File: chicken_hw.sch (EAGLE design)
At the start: 20 parts, among them U1 MUX-74HC4067SMD

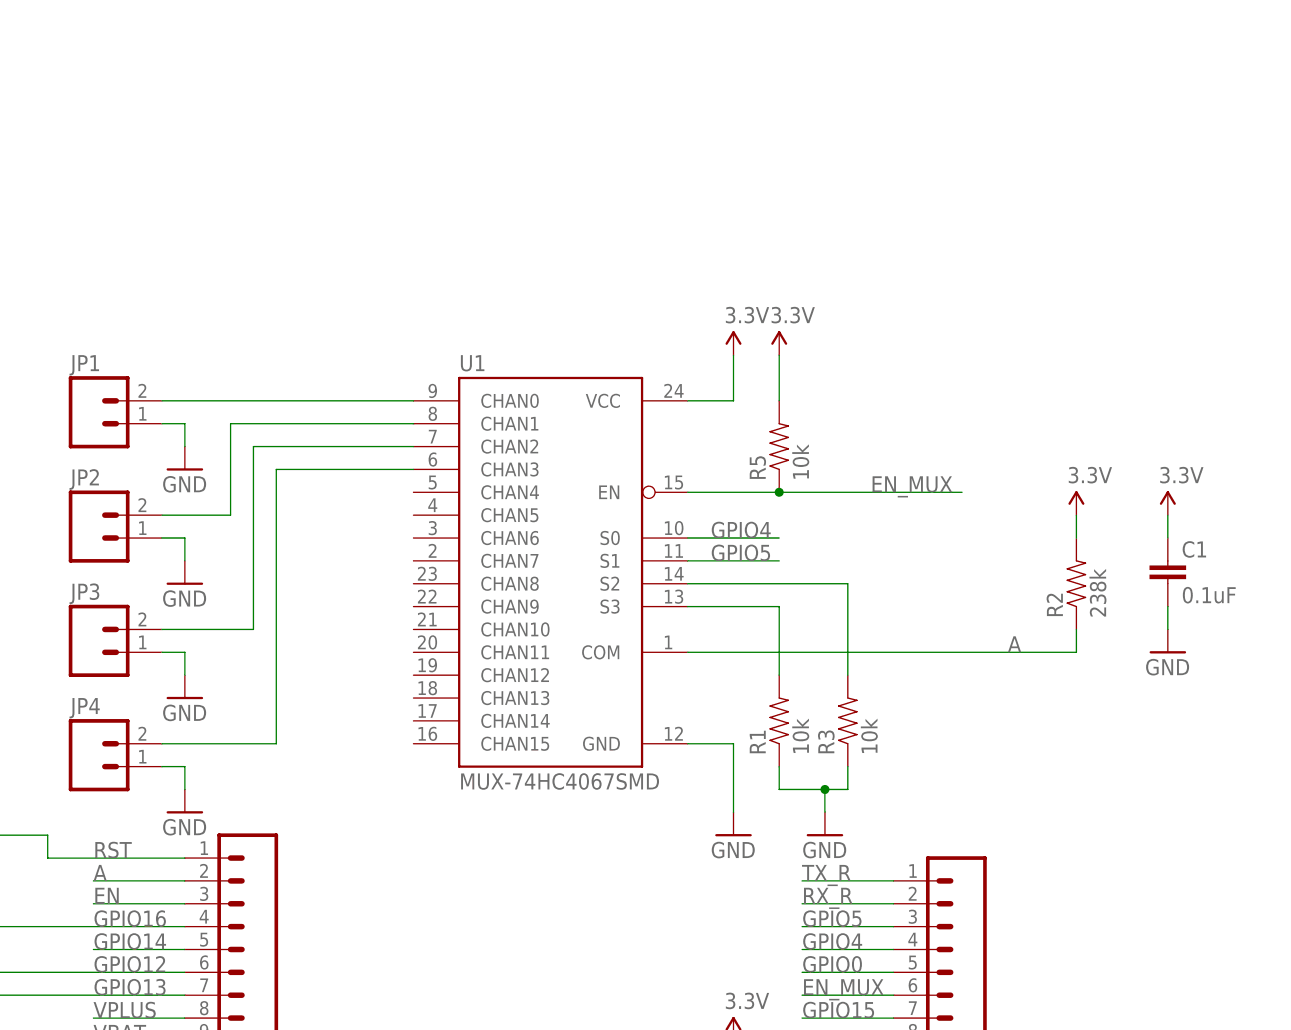
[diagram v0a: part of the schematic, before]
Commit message: Switch to 8to1 mux to save on cost
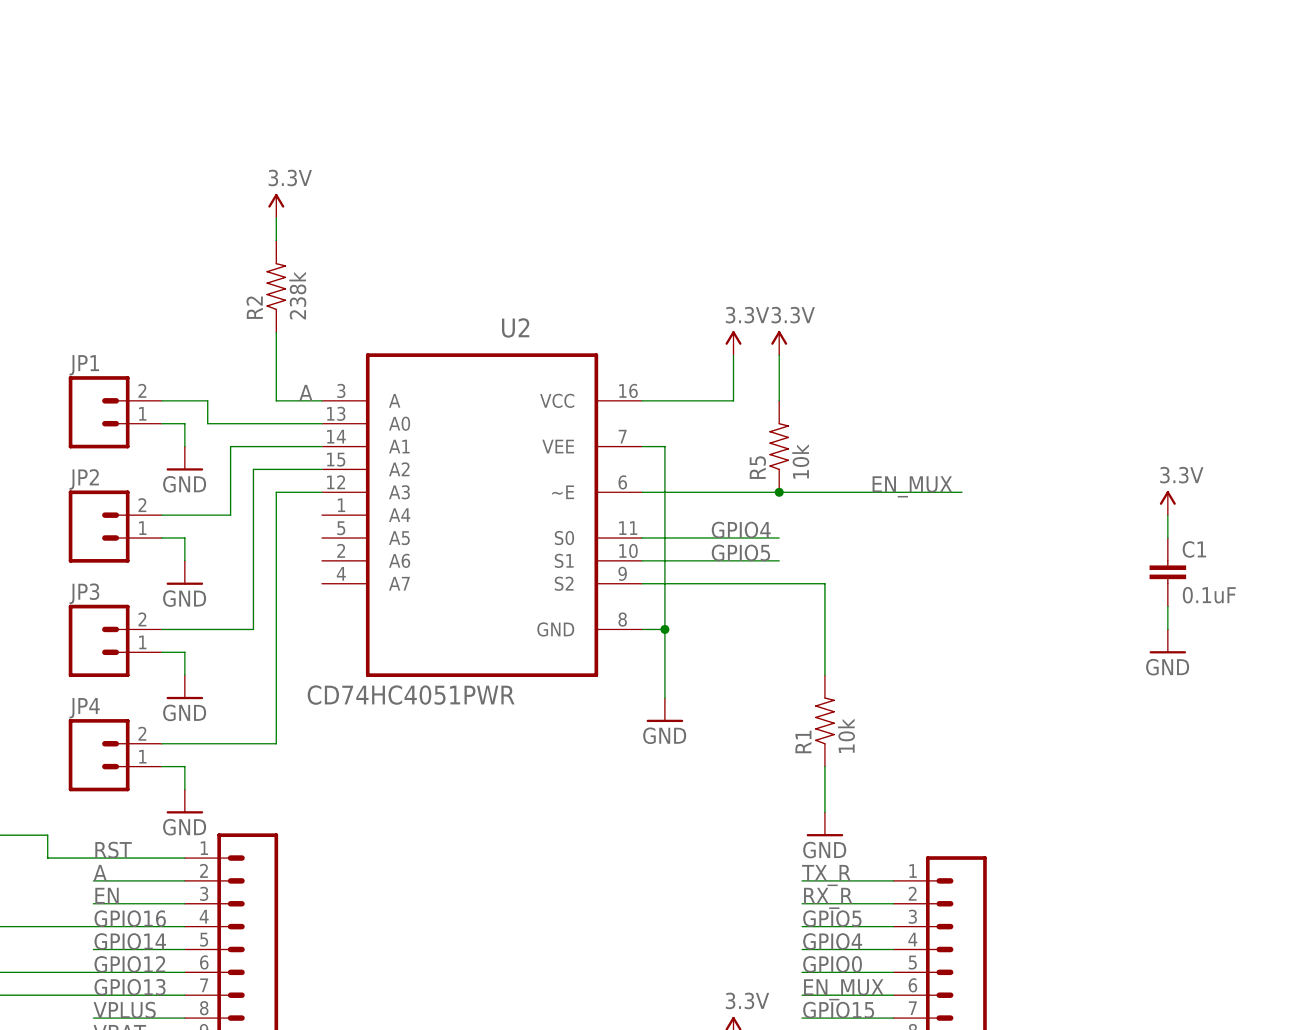
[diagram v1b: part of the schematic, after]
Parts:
- removed R3: 10k, SparkFun-Resistors:RESISTOR0603
- removed U1: MUX-74HC4067SMD, SparkFun-AnalogIC:MUX-74HC4067SMD
- added U2: CD74HC4051PWR, Texas Instruments_By_element14_Batch_1:CD74HC4051PWR
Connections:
- removed net N$6: R3.2, U1.S2
- net 3.3V: no longer U1.VCC
- net A: now also U2.A; no longer U1.COM
- net EN_MUX: now also U2.~E; no longer U1.EN
- net GND: now also U2.GND, U2.VEE; no longer R3.1, U1.GND
- net GPIO4: now also U2.S0; no longer U1.S0
- net GPIO5: now also U2.S1; no longer U1.S1
- net N$1: no longer U1.S3
- net N$2: now also U2.A0; no longer U1.CHAN0
- net N$3: now also U2.A1; no longer U1.CHAN1
- net N$4: now also U2.A2; no longer U1.CHAN2
- net N$5: now also U2.A3; no longer U1.CHAN3
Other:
- moved on the sheet: R1, R2
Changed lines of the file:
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@@
 <part name="GND3" library="SparkFun-Aesthetics" deviceset="GND" device=""/>
 <part name="SUPPLY1" library="SparkFun-Aesthetics" deviceset="3.3V" device=""/>
-<part name="U1" library="SparkFun-AnalogIC" deviceset="MUX-74HC4067" device="SMD"/>
 <part name="SUPPLY2" library="SparkFun-Aesthetics" deviceset="3.3V" device=""/>
 <part name="GND4" library="SparkFun-Aesthetics" deviceset="GND" device=""/>
@@
 <part name="R5" library="SparkFun-Resistors" deviceset="RESISTOR" device="0603" value="10k"/>
 <part name="R1" library="SparkFun-Resistors" deviceset="RESISTOR" device="0603" value="10k"/>
-<part name="R3" library="SparkFun-Resistors" deviceset="RESISTOR" device="0603" value="10k"/>
 <part name="R2" library="SparkFun-Resistors" deviceset="RESISTOR" device="0603" value="238k"/>
 <part name="D1" library="SparkFun-LED" deviceset="LED-GREEN" device="0603" value="GREEN"/>
@@
 <part name="LOGO1" library="SparkFun-Aesthetics" deviceset="OSHW-LOGO" device="S"/>
 <part name="DS" library="SparkFun-Passives" deviceset="JUMPER-PAD-2-NC_BY_TRACE" device=""/>
+<part name="U2" library="Texas Instruments_By_element14_Batch_1" deviceset="CD74HC4051PWR" device=""/>
 </parts>
 <sheets>
@@
 <instance part="GND3" gate="1" x="-15.24" y="17.78"/>
 <instance part="SUPPLY1" gate="G$1" x="60.96" y="25.4"/>
-<instance part="U1" gate="G$1" x="40.64" y="78.74"/>
 <instance part="SUPPLY2" gate="G$1" x="60.96" y="101.6"/>
-<instance part="GND4" gate="1" x="60.96" y="48.26"/>
+<instance part="GND4" gate="1" x="53.34" y="60.96"/>
 <instance part="SUPPLY3" gate="G$1" x="66.04" y="101.6"/>
-<instance part="SUPPLY4" gate="G$1" x="99.06" y="83.82"/>
+<instance part="SUPPLY4" gate="G$1" x="10.16" y="116.84"/>
 <instance part="JP1" gate="G$1" x="-10.16" y="93.98"/>
 <instance part="JP2" gate="G$1" x="-10.16" y="81.28"/>
@@
 <instance part="C1" gate="G$1" x="109.22" y="76.2"/>
 <instance part="R5" gate="G$1" x="66.04" y="91.44" rot="R90"/>
-<instance part="R1" gate="G$1" x="66.04" y="60.96" rot="R90"/>
-<instance part="R3" gate="G$1" x="73.66" y="60.96" rot="R90"/>
-<instance part="R2" gate="G$1" x="99.06" y="76.2" rot="R90"/>
+<instance part="R1" gate="G$1" x="71.12" y="60.96" rot="R90"/>
+<instance part="R2" gate="G$1" x="10.16" y="109.22" rot="R90"/>
 <instance part="D1" gate="G$1" x="-53.34" y="10.16"/>
 <instance part="D2" gate="G$1" x="-40.64" y="10.16"/>
@@
 <instance part="LOGO1" gate="G$1" x="137.16" y="12.7"/>
 <instance part="DS" gate="G$1" x="-27.94" y="43.18" rot="R90"/>
+<instance part="U2" gate="A" x="33.02" y="86.36" rot="MR0"/>
 </instances>
 <busses>
@@
 </segment>
 <segment>
-<pinref part="U1" gate="G$1" pin="COM"/>
-<wire x1="55.88" y1="68.58" x2="99.06" y2="68.58" width="0.1524" layer="91"/>
-<label x="91.44" y="68.58" size="1.778" layer="95"/>
-<wire x1="99.06" y1="68.58" x2="99.06" y2="71.12" width="0.1524" layer="91"/>
+<wire x1="10.16" y1="96.52" x2="10.16" y2="104.14" width="0.1524" layer="91"/>
+<label x="12.7" y="96.52" size="1.778" layer="95"/>
 <pinref part="R2" gate="G$1" pin="1"/>
+<pinref part="U2" gate="A" pin="A"/>
+<wire x1="10.16" y1="96.52" x2="15.24" y2="96.52" width="0.1524" layer="91"/>
 </segment>
 </net>
@@
 </segment>
 <segment>
-<pinref part="U1" gate="G$1" pin="S0"/>
-<wire x1="55.88" y1="81.28" x2="66.04" y2="81.28" width="0.1524" layer="91"/>
+<wire x1="50.8" y1="81.28" x2="66.04" y2="81.28" width="0.1524" layer="91"/>
 <label x="58.42" y="81.28" size="1.778" layer="95"/>
+<pinref part="U2" gate="A" pin="S0"/>
 </segment>
 </net>
@@
 </segment>
 <segment>
-<pinref part="U1" gate="G$1" pin="S1"/>
-<wire x1="55.88" y1="78.74" x2="66.04" y2="78.74" width="0.1524" layer="91"/>
+<wire x1="50.8" y1="78.74" x2="66.04" y2="78.74" width="0.1524" layer="91"/>
 <label x="58.42" y="78.74" size="1.778" layer="95"/>
+<pinref part="U2" gate="A" pin="S1"/>
 </segment>
 </net>
@@
 </segment>
 <segment>
-<pinref part="U1" gate="G$1" pin="GND"/>
-<wire x1="55.88" y1="58.42" x2="60.96" y2="58.42" width="0.1524" layer="91"/>
-<pinref part="GND4" gate="1" pin="GND"/>
-<wire x1="60.96" y1="58.42" x2="60.96" y2="50.8" width="0.1524" layer="91"/>
-</segment>
-<segment>
 <pinref part="JP1" gate="G$1" pin="1"/>
 <wire x1="-2.54" y1="93.98" x2="0" y2="93.98" width="0.1524" layer="91"/>
@@
 </segment>
 <segment>
-<wire x1="66.04" y1="55.88" x2="66.04" y2="53.34" width="0.1524" layer="91"/>
-<wire x1="66.04" y1="53.34" x2="71.12" y2="53.34" width="0.1524" layer="91"/>
 <pinref part="GND9" gate="1" pin="GND"/>
-<wire x1="71.12" y1="53.34" x2="73.66" y2="53.34" width="0.1524" layer="91"/>
-<wire x1="73.66" y1="53.34" x2="73.66" y2="55.88" width="0.1524" layer="91"/>
-<wire x1="71.12" y1="50.8" x2="71.12" y2="53.34" width="0.1524" layer="91"/>
-<junction x="71.12" y="53.34"/>
+<wire x1="71.12" y1="50.8" x2="71.12" y2="55.88" width="0.1524" layer="91"/>
 <pinref part="R1" gate="G$1" pin="1"/>
-<pinref part="R3" gate="G$1" pin="1"/>
 </segment>
 <segment>
@@
 <wire x1="-40.64" y1="0" x2="-40.64" y2="5.08" width="0.1524" layer="91"/>
 </segment>
+<segment>
+<pinref part="U2" gate="A" pin="GND"/>
+<wire x1="50.8" y1="71.12" x2="53.34" y2="71.12" width="0.1524" layer="91"/>
+<pinref part="GND4" gate="1" pin="GND"/>
+<wire x1="53.34" y1="71.12" x2="53.34" y2="63.5" width="0.1524" layer="91"/>
+<wire x1="53.34" y1="71.12" x2="53.34" y2="91.44" width="0.1524" layer="91"/>
+<junction x="53.34" y="71.12"/>
+<pinref part="U2" gate="A" pin="VEE"/>
+<wire x1="53.34" y1="91.44" x2="50.8" y2="91.44" width="0.1524" layer="91"/>
+</segment>
 </net>
 <net name="N$11" class="0">
@@
 </segment>
 <segment>
-<pinref part="U1" gate="G$1" pin="VCC"/>
-<wire x1="55.88" y1="96.52" x2="60.96" y2="96.52" width="0.1524" layer="91"/>
+<wire x1="50.8" y1="96.52" x2="60.96" y2="96.52" width="0.1524" layer="91"/>
 <pinref part="SUPPLY2" gate="G$1" pin="3.3V"/>
 <wire x1="60.96" y1="96.52" x2="60.96" y2="101.6" width="0.1524" layer="91"/>
@@
 <segment>
 <pinref part="SUPPLY4" gate="G$1" pin="3.3V"/>
-<wire x1="99.06" y1="83.82" x2="99.06" y2="81.28" width="0.1524" layer="91"/>
+<wire x1="10.16" y1="116.84" x2="10.16" y2="114.3" width="0.1524" layer="91"/>
 <pinref part="R2" gate="G$1" pin="2"/>
 </segment>
@@
 <net name="EN_MUX" class="0">
 <segment>
-<pinref part="U1" gate="G$1" pin="EN"/>
-<wire x1="55.88" y1="86.36" x2="66.04" y2="86.36" width="0.1524" layer="91"/>
+<wire x1="50.8" y1="86.36" x2="66.04" y2="86.36" width="0.1524" layer="91"/>
 <label x="76.2" y="86.36" size="1.778" layer="95"/>
 <pinref part="R5" gate="G$1" pin="1"/>
 <wire x1="66.04" y1="86.36" x2="86.36" y2="86.36" width="0.1524" layer="91"/>
 <junction x="66.04" y="86.36"/>
+<pinref part="U2" gate="A" pin="~E"/>
 </segment>
 <segment>
@@
 </segment>
 </net>
-<net name="N$2" class="0">
-<segment>
-<pinref part="JP1" gate="G$1" pin="2"/>
-<pinref part="U1" gate="G$1" pin="CHAN0"/>
-<wire x1="-2.54" y1="96.52" x2="25.4" y2="96.52" width="0.1524" layer="91"/>
-</segment>
-</net>
 <net name="N$3" class="0">
 <segment>
 <pinref part="JP2" gate="G$1" pin="2"/>
 <wire x1="-2.54" y1="83.82" x2="5.08" y2="83.82" width="0.1524" layer="91"/>
-<wire x1="5.08" y1="83.82" x2="5.08" y2="93.98" width="0.1524" layer="91"/>
-<pinref part="U1" gate="G$1" pin="CHAN1"/>
-<wire x1="5.08" y1="93.98" x2="25.4" y2="93.98" width="0.1524" layer="91"/>
+<wire x1="5.08" y1="83.82" x2="5.08" y2="91.44" width="0.1524" layer="91"/>
+<pinref part="U2" gate="A" pin="A1"/>
+<wire x1="5.08" y1="91.44" x2="15.24" y2="91.44" width="0.1524" layer="91"/>
 </segment>
 </net>
@@
 <pinref part="JP3" gate="G$1" pin="2"/>
 <wire x1="-2.54" y1="71.12" x2="7.62" y2="71.12" width="0.1524" layer="91"/>
-<wire x1="7.62" y1="71.12" x2="7.62" y2="91.44" width="0.1524" layer="91"/>
-<pinref part="U1" gate="G$1" pin="CHAN2"/>
-<wire x1="7.62" y1="91.44" x2="25.4" y2="91.44" width="0.1524" layer="91"/>
+<wire x1="7.62" y1="71.12" x2="7.62" y2="88.9" width="0.1524" layer="91"/>
+<pinref part="U2" gate="A" pin="A2"/>
+<wire x1="7.62" y1="88.9" x2="15.24" y2="88.9" width="0.1524" layer="91"/>
 </segment>
 </net>
@@
 <pinref part="JP4" gate="G$1" pin="2"/>
 <wire x1="-2.54" y1="58.42" x2="10.16" y2="58.42" width="0.1524" layer="91"/>
-<wire x1="10.16" y1="58.42" x2="10.16" y2="88.9" width="0.1524" layer="91"/>
-<pinref part="U1" gate="G$1" pin="CHAN3"/>
-<wire x1="10.16" y1="88.9" x2="25.4" y2="88.9" width="0.1524" layer="91"/>
+<wire x1="10.16" y1="58.42" x2="10.16" y2="86.36" width="0.1524" layer="91"/>
+<pinref part="U2" gate="A" pin="A3"/>
+<wire x1="10.16" y1="86.36" x2="15.24" y2="86.36" width="0.1524" layer="91"/>
 </segment>
 </net>
 <net name="N$1" class="0">
 <segment>
-<pinref part="U1" gate="G$1" pin="S3"/>
-<wire x1="55.88" y1="73.66" x2="66.04" y2="73.66" width="0.1524" layer="91"/>
-<wire x1="66.04" y1="73.66" x2="66.04" y2="66.04" width="0.1524" layer="91"/>
+<wire x1="50.8" y1="76.2" x2="71.12" y2="76.2" width="0.1524" layer="91"/>
+<wire x1="71.12" y1="76.2" x2="71.12" y2="66.04" width="0.1524" layer="91"/>
 <pinref part="R1" gate="G$1" pin="2"/>
-</segment>
-</net>
-<net name="N$6" class="0">
-<segment>
-<pinref part="U1" gate="G$1" pin="S2"/>
-<wire x1="55.88" y1="76.2" x2="73.66" y2="76.2" width="0.1524" layer="91"/>
-<wire x1="73.66" y1="76.2" x2="73.66" y2="66.04" width="0.1524" layer="91"/>
-<pinref part="R3" gate="G$1" pin="2"/>
 </segment>
 </net>
@@
 </segment>
 </net>
+<net name="N$2" class="0">
+<segment>
+<pinref part="JP1" gate="G$1" pin="2"/>
+<wire x1="-2.54" y1="96.52" x2="2.54" y2="96.52" width="0.1524" layer="91"/>
+<wire x1="2.54" y1="96.52" x2="2.54" y2="93.98" width="0.1524" layer="91"/>
+<pinref part="U2" gate="A" pin="A0"/>
+<wire x1="2.54" y1="93.98" x2="15.24" y2="93.98" width="0.1524" layer="91"/>
+</segment>
+</net>

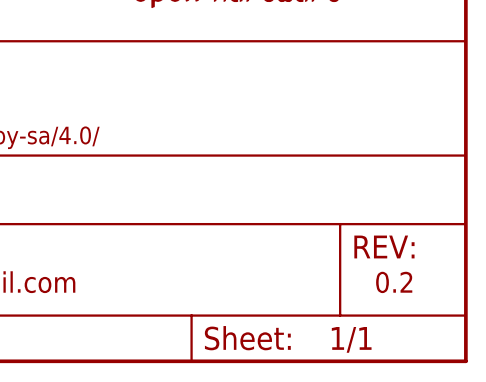
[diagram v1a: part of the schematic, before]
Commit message: Fully routed 8:1 mux, ready for production
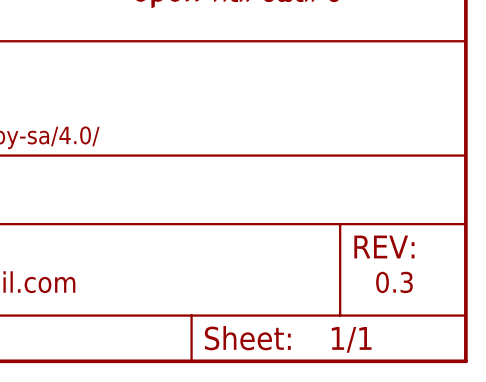
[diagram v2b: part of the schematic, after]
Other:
- note added: "0.3"
- note removed: "0.2"
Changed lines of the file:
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@@
 jason.k.holden@gmail.com</text>
 <text x="-33.02" y="35.56" size="1.778" layer="94" rot="R90">Enable Deep Sleep</text>
-<text x="152.4" y="-27.94" size="2.286" layer="94" font="vector" ratio="12">0.2</text>
+<text x="152.4" y="-27.94" size="2.286" layer="94" font="vector" ratio="12">0.3</text>
 </plain>
 <instances>

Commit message: Fix ERC errors w/ V0.3 board  VCC and S2 not connected (unrouted)
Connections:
- net 3.3V: now also U2.VCC
- net N$1: now also U2.S2
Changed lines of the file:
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@@
 </segment>
 <segment>
-<wire x1="50.8" y1="96.52" x2="60.96" y2="96.52" width="0.1524" layer="91"/>
 <pinref part="SUPPLY2" gate="G$1" pin="3.3V"/>
 <wire x1="60.96" y1="96.52" x2="60.96" y2="101.6" width="0.1524" layer="91"/>
+<pinref part="U2" gate="A" pin="VCC"/>
+<wire x1="50.8" y1="96.52" x2="60.96" y2="96.52" width="0.1524" layer="91"/>
 </segment>
 <segment>
@@
 <net name="N$1" class="0">
 <segment>
-<wire x1="50.8" y1="76.2" x2="71.12" y2="76.2" width="0.1524" layer="91"/>
 <wire x1="71.12" y1="76.2" x2="71.12" y2="66.04" width="0.1524" layer="91"/>
 <pinref part="R1" gate="G$1" pin="2"/>
+<pinref part="U2" gate="A" pin="S2"/>
+<wire x1="50.8" y1="76.2" x2="71.12" y2="76.2" width="0.1524" layer="91"/>
 </segment>
 </net>

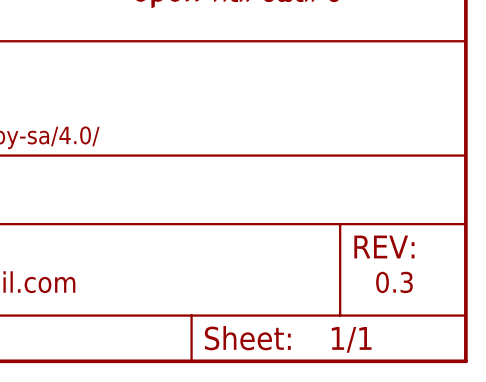
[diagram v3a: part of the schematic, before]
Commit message: Rev silkscreen to ver 0.4
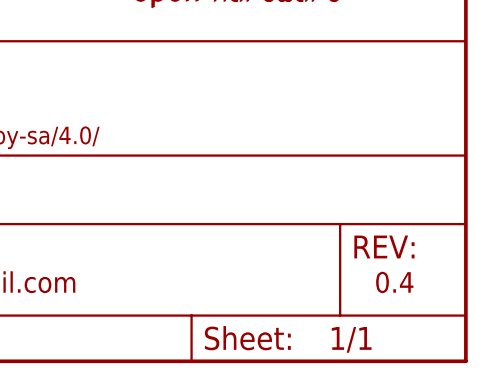
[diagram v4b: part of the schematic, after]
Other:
- note added: "0.4"
- note removed: "0.3"
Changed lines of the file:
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@@
 jason.k.holden@gmail.com</text>
 <text x="-33.02" y="35.56" size="1.778" layer="94" rot="R90">Enable Deep Sleep</text>
-<text x="152.4" y="-27.94" size="2.286" layer="94" font="vector" ratio="12">0.3</text>
+<text x="152.4" y="-27.94" size="2.286" layer="94" font="vector" ratio="12">0.4</text>
 </plain>
 <instances>
